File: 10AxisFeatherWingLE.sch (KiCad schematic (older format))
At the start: 19 parts, among them J1 feather long, J2 feather short, J3 grove connector, J4 feather long, J5 feather short, J6 feather breakout, U1 LSM9DS1, U2 BMP280

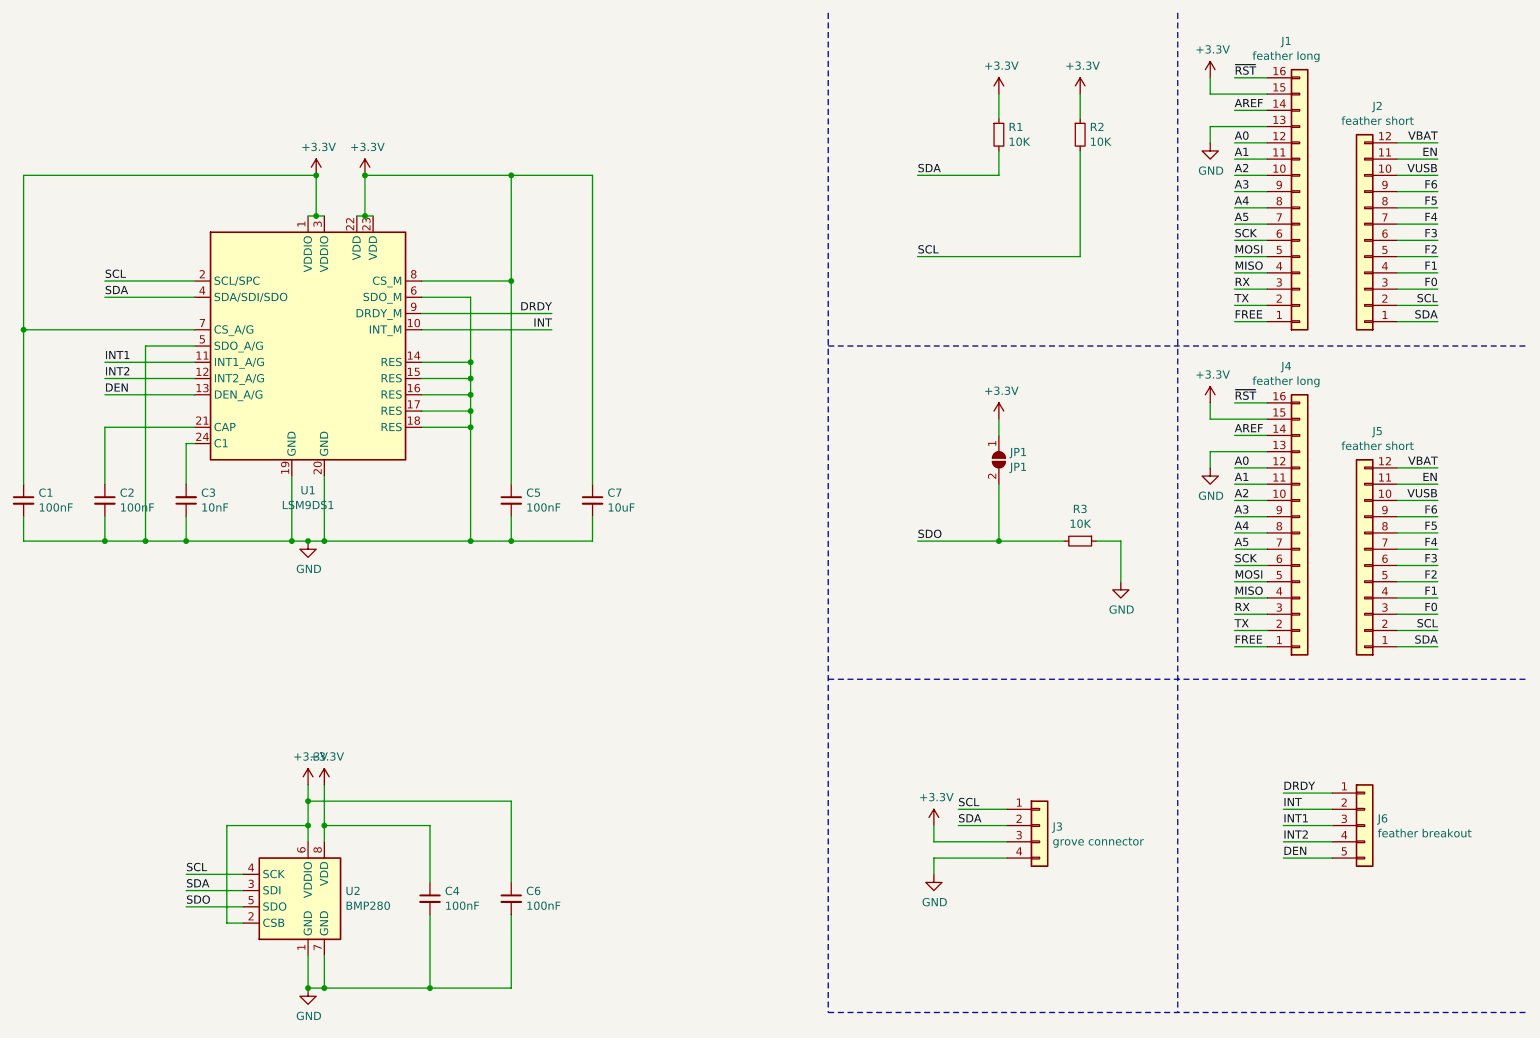
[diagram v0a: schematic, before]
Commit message: Corrected capacitor values
CAP and C1 capacitors were flipped, fixed
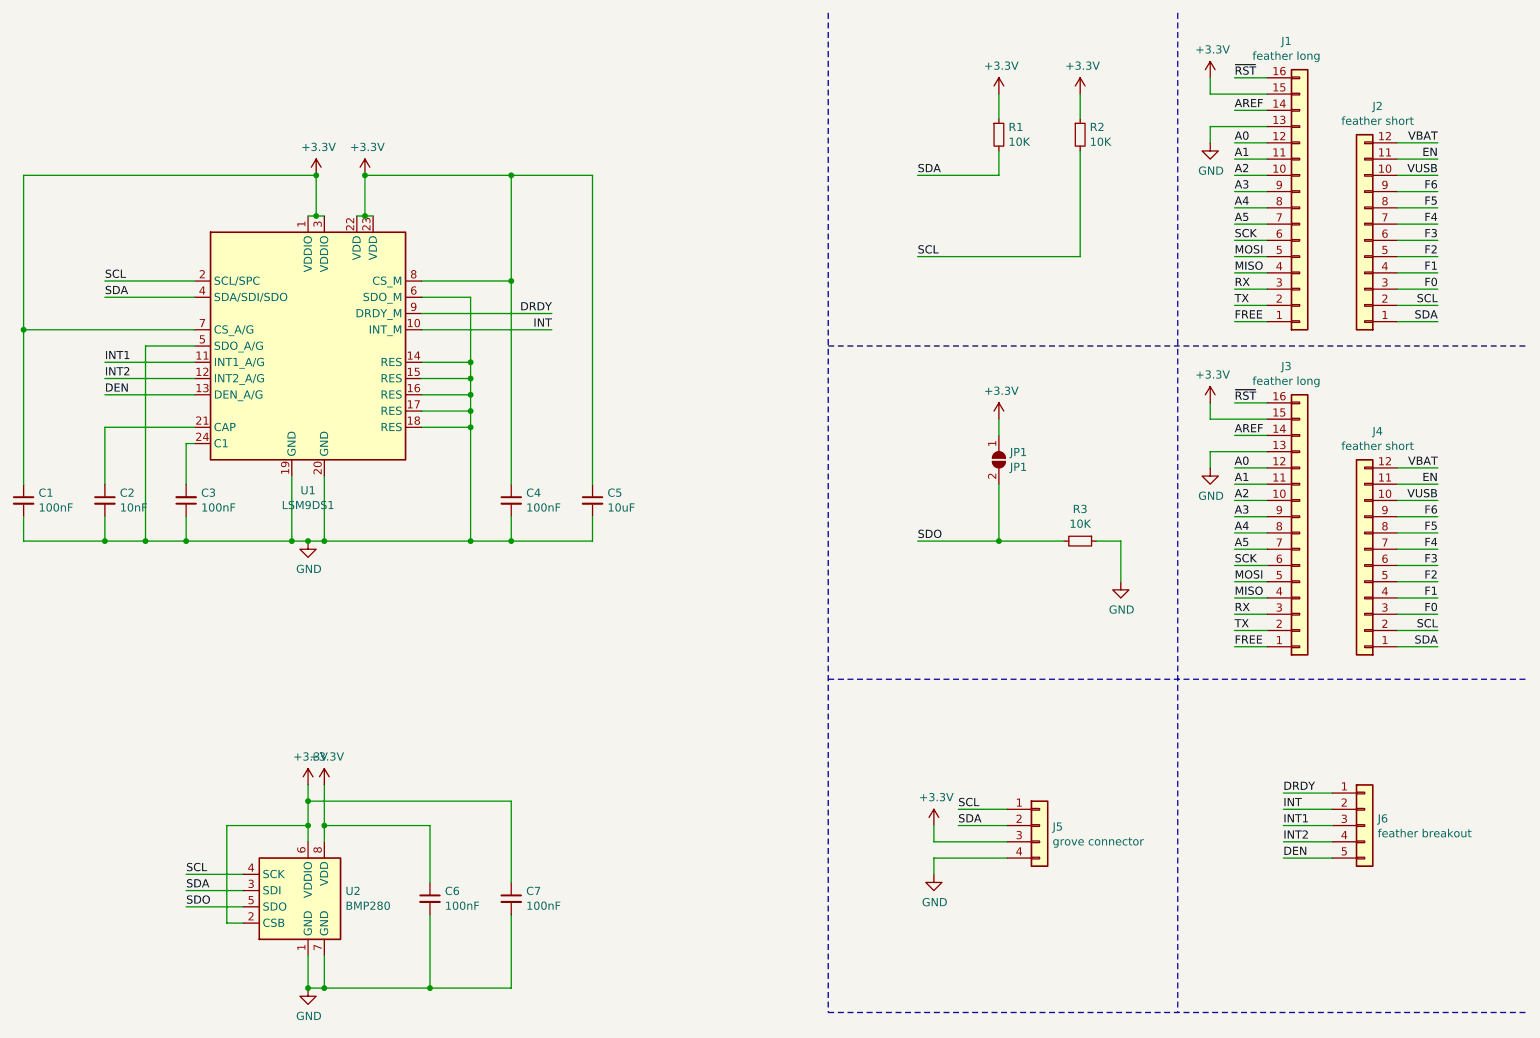
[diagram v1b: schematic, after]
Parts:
- C2: value 100nF -> 10nF
- C3: value 10nF -> 100nF
- J3: renamed from J4; footprint Connector_PinHeader_2.54mm:PinHeader_1x16_P2.54mm_Vertical -> Connector_PinSocket_2.54mm:PinSocket_1x16_P2.54mm_Vertical
- J4: renamed from J5; footprint Connector_PinHeader_2.54mm:PinHeader_1x12_P2.54mm_Vertical -> Connector_PinSocket_2.54mm:PinSocket_1x12_P2.54mm_Vertical
- renumbered C5 to C4, C7 to C5, C4 to C6, C6 to C7, J3 to J5
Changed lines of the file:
@@
 $EndComp
 $Comp
-L power:GND #PWR02
+L power:GND #PWR04
 U 1 1 5D3787E4
 P 8550 1300
-F 0 "#PWR02" H 8550 1050 50  0001 C CNN
+F 0 "#PWR04" H 8550 1050 50  0001 C CNN
 F 1 "GND" H 8555 1127 50  0000 C CNN
 F 2 "" H 8550 1300 50  0001 C CNN
@@
 	6200 500  6200 6650
 $Comp
-L Connector_Generic:Conn_01x16 J4
+L Connector_Generic:Conn_01x16 J3
 U 1 1 5E0C551A
 P 9100 3700
-F 0 "J4" H 9019 2675 50  0000 C CNN
+F 0 "J3" H 9019 2675 50  0000 C CNN
 F 1 "feather long" H 9019 2766 50  0000 C CNN
-F 2 "Connector_PinHeader_2.54mm:PinHeader_1x16_P2.54mm_Vertical" H 9100 3700 50  0001 C CNN
+F 2 "Connector_PinSocket_2.54mm:PinSocket_1x16_P2.54mm_Vertical" H 9100 3700 50  0001 C CNN
 F 3 "~" H 9100 3700 50  0001 C CNN
 	1    9100 3700
@@
 $EndComp
 $Comp
-L Connector_Generic:Conn_01x12 J5
+L Connector_Generic:Conn_01x12 J4
 U 1 1 5E0C5520
 P 9500 3900
-F 0 "J5" H 9420 3075 50  0000 C CNN
+F 0 "J4" H 9420 3075 50  0000 C CNN
 F 1 "feather short" H 9420 3166 50  0000 C CNN
-F 2 "Connector_PinHeader_2.54mm:PinHeader_1x12_P2.54mm_Vertical" H 9500 3900 50  0001 C CNN
+F 2 "Connector_PinSocket_2.54mm:PinSocket_1x12_P2.54mm_Vertical" H 9500 3900 50  0001 C CNN
 F 3 "~" H 9500 3900 50  0001 C CNN
 	1    9500 3900
@@
 	9700 4400 9950 4400
 $Comp
-L power:+3.3V #PWR015
+L power:+3.3V #PWR07
 U 1 1 5E0C555A
 P 8550 2900
-F 0 "#PWR015" H 8550 2750 50  0001 C CNN
+F 0 "#PWR07" H 8550 2750 50  0001 C CNN
 F 1 "+3.3V" H 8565 3073 50  0000 C CNN
 F 2 "" H 8550 2900 50  0001 C CNN
@@
 $EndComp
 $Comp
-L power:GND #PWR016
+L power:GND #PWR09
 U 1 1 5E0C5560
 P 8550 3300
-F 0 "#PWR016" H 8550 3050 50  0001 C CNN
+F 0 "#PWR09" H 8550 3050 50  0001 C CNN
 F 1 "GND" H 8555 3127 50  0000 C CNN
 F 2 "" H 8550 3300 50  0001 C CNN
@@
 P 2250 3500
 F 0 "C3" H 2158 3454 50  0000 R CNN
-F 1 "10nF" H 2158 3545 50  0000 R CNN
+F 1 "100nF" H 2158 3545 50  0000 R CNN
 F 2 "Capacitor_SMD:C_0603_1608Metric" H 2250 3500 50  0001 C CNN
 F 3 "~" H 2250 3500 50  0001 C CNN
@@
 P 1750 3500
 F 0 "C2" H 1842 3546 50  0000 L CNN
-F 1 "100nF" H 1842 3455 50  0000 L CNN
+F 1 "10nF" H 1842 3455 50  0000 L CNN
 F 2 "Capacitor_SMD:C_0603_1608Metric" H 1750 3500 50  0001 C CNN
 F 3 "~" H 1750 3500 50  0001 C CNN
@@
 	1750 3050 1750 3400
 $Comp
-L Device:C_Small C5
+L Device:C_Small C4
 U 1 1 5E10D342
 P 4250 3500
-F 0 "C5" H 4342 3546 50  0000 L CNN
+F 0 "C4" H 4342 3546 50  0000 L CNN
 F 1 "100nF" H 4342 3455 50  0000 L CNN
 F 2 "Capacitor_SMD:C_0603_1608Metric" H 4250 3500 50  0001 C CNN
@@
 $EndComp
 $Comp
-L Device:C_Small C7
+L Device:C_Small C5
 U 1 1 5E1105B8
 P 4750 3500
-F 0 "C7" H 4842 3546 50  0000 L CNN
+F 0 "C5" H 4842 3546 50  0000 L CNN
 F 1 "10uF" H 4842 3455 50  0000 L CNN
 F 2 "Capacitor_SMD:C_0603_1608Metric" H 4750 3500 50  0001 C CNN
@@
 	3050 1500 1250 1500
 $Comp
-L power:+3.3V #PWR08
+L power:+3.3V #PWR06
 U 1 1 5E11B1B7
 P 3350 1500
-F 0 "#PWR08" H 3350 1350 50  0001 C CNN
+F 0 "#PWR06" H 3350 1350 50  0001 C CNN
 F 1 "+3.3V" H 3365 1673 50  0000 C CNN
 F 2 "" H 3350 1500 50  0001 C CNN
@@
 $EndComp
 $Comp
-L power:+3.3V #PWR06
+L power:+3.3V #PWR05
 U 1 1 5E11AD9E
 P 3050 1500
-F 0 "#PWR06" H 3050 1350 50  0001 C CNN
+F 0 "#PWR05" H 3050 1350 50  0001 C CNN
 F 1 "+3.3V" H 3065 1673 50  0000 C CNN
 F 2 "" H 3050 1500 50  0001 C CNN
@@
 	1250 1500 1250 2450
 $Comp
-L power:GND #PWR03
+L power:GND #PWR010
 U 1 1 5E0C71B1
 P 3000 3750
-F 0 "#PWR03" H 3000 3500 50  0001 C CNN
+F 0 "#PWR010" H 3000 3500 50  0001 C CNN
 F 1 "GND" H 3005 3577 50  0000 C CNN
 F 2 "" H 3000 3750 50  0001 C CNN
@@
 	3000 3750 3100 3750
 $Comp
-L Device:C_Small C4
+L Device:C_Small C6
 U 1 1 5E1BEDBD
 P 3750 5950
-F 0 "C4" H 3842 5996 50  0000 L CNN
+F 0 "C6" H 3842 5996 50  0000 L CNN
 F 1 "100nF" H 3842 5905 50  0000 L CNN
 F 2 "Capacitor_SMD:C_0603_1608Metric" H 3750 5950 50  0001 C CNN
@@
 $EndComp
 $Comp
-L Device:C_Small C6
+L Device:C_Small C7
 U 1 1 5E1BF420
 P 4250 5950
-F 0 "C6" H 4342 5996 50  0000 L CNN
+F 0 "C7" H 4342 5996 50  0000 L CNN
 F 1 "100nF" H 4342 5905 50  0000 L CNN
 F 2 "Capacitor_SMD:C_0603_1608Metric" H 4250 5950 50  0001 C CNN
@@
 $EndComp
 $Comp
-L power:+3.3V #PWR04
+L power:+3.3V #PWR012
 U 1 1 5E1BF745
 P 3000 5250
-F 0 "#PWR04" H 3000 5100 50  0001 C CNN
+F 0 "#PWR012" H 3000 5100 50  0001 C CNN
 F 1 "+3.3V" H 3015 5423 50  0000 C CNN
 F 2 "" H 3000 5250 50  0001 C CNN
@@
 $EndComp
 $Comp
-L power:+3.3V #PWR07
+L power:+3.3V #PWR013
 U 1 1 5E1BFA3F
 P 3100 5250
-F 0 "#PWR07" H 3100 5100 50  0001 C CNN
+F 0 "#PWR013" H 3100 5100 50  0001 C CNN
 F 1 "+3.3V" H 3115 5423 50  0000 C CNN
 F 2 "" H 3100 5250 50  0001 C CNN
@@
 Connection ~ 3750 6500
 $Comp
-L power:GND #PWR05
+L power:GND #PWR016
 U 1 1 5E1E9755
 P 3000 6500
-F 0 "#PWR05" H 3000 6250 50  0001 C CNN
+F 0 "#PWR016" H 3000 6250 50  0001 C CNN
 F 1 "GND" H 3005 6327 50  0000 C CNN
 F 2 "" H 3000 6500 50  0001 C CNN
@@
 	3750 5500 3750 5850
 $Comp
-L power:+3.3V #PWR011
+L power:+3.3V #PWR02
 U 1 1 5E25A615
 P 7250 1000
-F 0 "#PWR011" H 7250 850 50  0001 C CNN
+F 0 "#PWR02" H 7250 850 50  0001 C CNN
 F 1 "+3.3V" H 7265 1173 50  0000 C CNN
 F 2 "" H 7250 1000 50  0001 C CNN
@@
 $EndComp
 $Comp
-L power:+3.3V #PWR013
+L power:+3.3V #PWR03
 U 1 1 5E25A95F
 P 7750 1000
-F 0 "#PWR013" H 7750 850 50  0001 C CNN
+F 0 "#PWR03" H 7750 850 50  0001 C CNN
 F 1 "+3.3V" H 7765 1173 50  0000 C CNN
 F 2 "" H 7750 1000 50  0001 C CNN
@@
 	7250 3750 7650 3750
 $Comp
-L power:+3.3V #PWR012
+L power:+3.3V #PWR08
 U 1 1 5E2A6AB5
 P 7250 3000
-F 0 "#PWR012" H 7250 2850 50  0001 C CNN
+F 0 "#PWR08" H 7250 2850 50  0001 C CNN
 F 1 "+3.3V" H 7265 3173 50  0000 C CNN
 F 2 "" H 7250 3000 50  0001 C CNN
@@
 $EndComp
 $Comp
-L power:GND #PWR014
+L power:GND #PWR011
 U 1 1 5E2A6E98
 P 8000 4000
-F 0 "#PWR014" H 8000 3750 50  0001 C CNN
+F 0 "#PWR011" H 8000 3750 50  0001 C CNN
 F 1 "GND" H 8005 3827 50  0000 C CNN
 F 2 "" H 8000 4000 50  0001 C CNN
@@
 SDO
 $Comp
-L Connector_Generic:Conn_01x04 J3
+L Connector_Generic:Conn_01x04 J5
 U 1 1 5E2B8C1A
 P 7500 5500
-F 0 "J3" H 7580 5492 50  0000 L CNN
+F 0 "J5" H 7580 5492 50  0000 L CNN
 F 1 "grove connector" H 7580 5401 50  0000 L CNN
 F 2 "Connector:NS-Tech_Grove_1x04_P2mm_Vertical" H 7500 5500 50  0001 C CNN
@@
 	6850 5700 7300 5700
 $Comp
-L power:+3.3V #PWR09
+L power:+3.3V #PWR014
 U 1 1 5E330536
 P 6850 5500
-F 0 "#PWR09" H 6850 5350 50  0001 C CNN
+F 0 "#PWR014" H 6850 5350 50  0001 C CNN
 F 1 "+3.3V" H 6865 5673 50  0000 C CNN
 F 2 "" H 6850 5500 50  0001 C CNN
@@
 $EndComp
 $Comp
-L power:GND #PWR010
+L power:GND #PWR015
 U 1 1 5E330953
 P 6850 5800
-F 0 "#PWR010" H 6850 5550 50  0001 C CNN
+F 0 "#PWR015" H 6850 5550 50  0001 C CNN
 F 1 "GND" H 6855 5627 50  0000 C CNN
 F 2 "" H 6850 5800 50  0001 C CNN

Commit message: Minor format fix
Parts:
- added H1, H2, H3, H4: MountingHole, MountingHole:MountingHole_2.7mm_M2.5, symbol Mechanical:MountingHole
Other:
- moved on the sheet: J6
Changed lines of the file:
@@
 L Connector_Generic:Conn_01x05 J6
 U 1 1 5E2059E9
-P 9500 5500
-F 0 "J6" H 9580 5542 50  0000 L CNN
-F 1 "feather breakout" H 9580 5451 50  0000 L CNN
-F 2 "Connector_PinHeader_2.54mm:PinHeader_1x05_P2.54mm_Vertical" H 9500 5500 50  0001 C CNN
-F 3 "~" H 9500 5500 50  0001 C CNN
-	1    9500 5500
-	1    0    0    -1
-$EndComp
-Text Label 9000 5300 0    50   ~ 0
+P 9550 5000
+F 0 "J6" H 9630 5042 50  0000 L CNN
+F 1 "feather breakout" H 9630 4951 50  0000 L CNN
+F 2 "Connector_PinHeader_2.54mm:PinHeader_1x05_P2.54mm_Vertical" H 9550 5000 50  0001 C CNN
+F 3 "~" H 9550 5000 50  0001 C CNN
+	1    9550 5000
+	1    0    0    -1
+$EndComp
+Text Label 9050 4800 0    50   ~ 0
 DRDY
-Text Label 9000 5400 0    50   ~ 0
+Text Label 9050 4900 0    50   ~ 0
 INT
-Text Label 9000 5500 0    50   ~ 0
+Text Label 9050 5000 0    50   ~ 0
 INT1
-Text Label 9000 5600 0    50   ~ 0
+Text Label 9050 5100 0    50   ~ 0
 INT2
-Text Label 9000 5700 0    50   ~ 0
+Text Label 9050 5200 0    50   ~ 0
 DEN
 Wire Wire Line
@@
 $EndComp
 Wire Wire Line
-	9000 5300 9300 5300
-Wire Wire Line
-	9000 5400 9300 5400
-Wire Wire Line
-	9000 5500 9300 5500
-Wire Wire Line
-	9000 5600 9300 5600
-Wire Wire Line
-	9000 5700 9300 5700
+	9050 4800 9350 4800
+Wire Wire Line
+	9050 4900 9350 4900
+Wire Wire Line
+	9050 5000 9350 5000
+Wire Wire Line
+	9050 5100 9350 5100
+Wire Wire Line
+	9050 5200 9350 5200
 Wire Wire Line
 	7000 5400 7300 5400
@@
 	1    0    0    -1
 $EndComp
+$Comp
+L Mechanical:MountingHole H1
+U 1 1 5E162FA6
+P 9250 5750
+F 0 "H1" H 9350 5796 50  0000 L CNN
+F 1 "MountingHole" H 9350 5705 50  0000 L CNN
+F 2 "MountingHole:MountingHole_2.7mm_M2.5" H 9250 5750 50  0001 C CNN
+F 3 "~" H 9250 5750 50  0001 C CNN
+	1    9250 5750
+	1    0    0    -1
+$EndComp
+$Comp
+L Mechanical:MountingHole H2
+U 1 1 5E163654
+P 9250 6000
+F 0 "H2" H 9350 6046 50  0000 L CNN
+F 1 "MountingHole" H 9350 5955 50  0000 L CNN
+F 2 "MountingHole:MountingHole_2.7mm_M2.5" H 9250 6000 50  0001 C CNN
+F 3 "~" H 9250 6000 50  0001 C CNN
+	1    9250 6000
+	1    0    0    -1
+$EndComp
+$Comp
+L Mechanical:MountingHole H3
+U 1 1 5E163A5D
+P 9250 6250
+F 0 "H3" H 9350 6296 50  0000 L CNN
+F 1 "MountingHole" H 9350 6205 50  0000 L CNN
+F 2 "MountingHole:MountingHole_2.7mm_M2.5" H 9250 6250 50  0001 C CNN
+F 3 "~" H 9250 6250 50  0001 C CNN
+	1    9250 6250
+	1    0    0    -1
+$EndComp
+$Comp
+L Mechanical:MountingHole H4
+U 1 1 5E163E72
+P 9250 6500
+F 0 "H4" H 9350 6546 50  0000 L CNN
+F 1 "MountingHole" H 9350 6455 50  0000 L CNN
+F 2 "MountingHole:MountingHole_2.7mm_M2.5" H 9250 6500 50  0001 C CNN
+F 3 "~" H 9250 6500 50  0001 C CNN
+	1    9250 6500
+	1    0    0    -1
+$EndComp
+Wire Notes Line
+	8350 5500 10500 5500
 $EndSCHEMATC

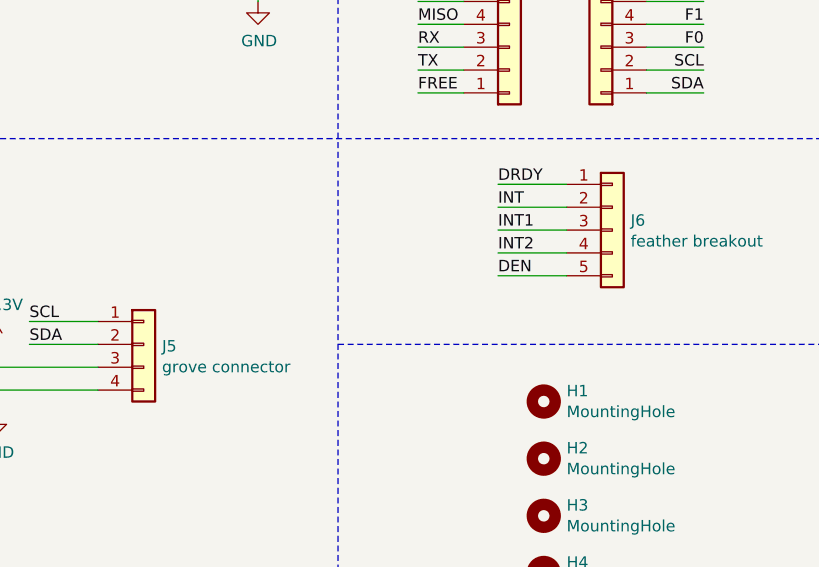
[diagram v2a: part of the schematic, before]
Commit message: Increased trace width
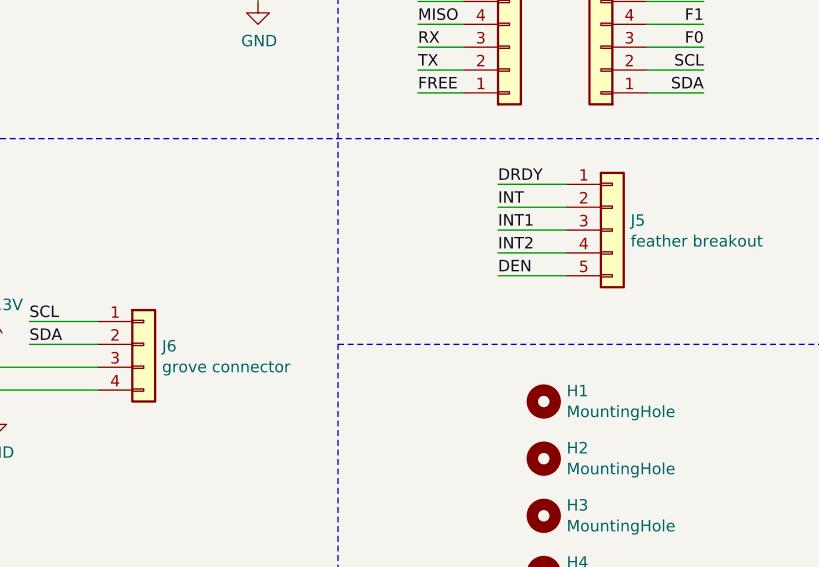
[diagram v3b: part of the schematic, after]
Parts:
- renumbered J6 to J5, J5 to J6
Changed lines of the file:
@@
 SDO
 $Comp
-L Connector_Generic:Conn_01x05 J6
+L Connector_Generic:Conn_01x05 J5
 U 1 1 5E2059E9
 P 9550 5000
-F 0 "J6" H 9630 5042 50  0000 L CNN
+F 0 "J5" H 9630 5042 50  0000 L CNN
 F 1 "feather breakout" H 9630 4951 50  0000 L CNN
 F 2 "Connector_PinHeader_2.54mm:PinHeader_1x05_P2.54mm_Vertical" H 9550 5000 50  0001 C CNN
@@
 SDO
 $Comp
-L Connector_Generic:Conn_01x04 J5
+L Connector_Generic:Conn_01x04 J6
 U 1 1 5E2B8C1A
 P 7500 5500
-F 0 "J5" H 7580 5492 50  0000 L CNN
+F 0 "J6" H 7580 5492 50  0000 L CNN
 F 1 "grove connector" H 7580 5401 50  0000 L CNN
 F 2 "Connector:NS-Tech_Grove_1x04_P2mm_Vertical" H 7500 5500 50  0001 C CNN

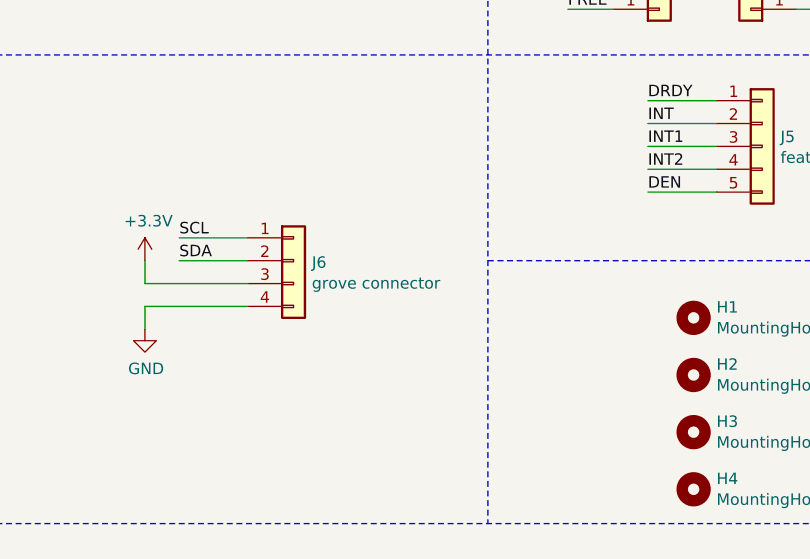
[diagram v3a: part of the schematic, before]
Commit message: Changed grove connector to STEMMA
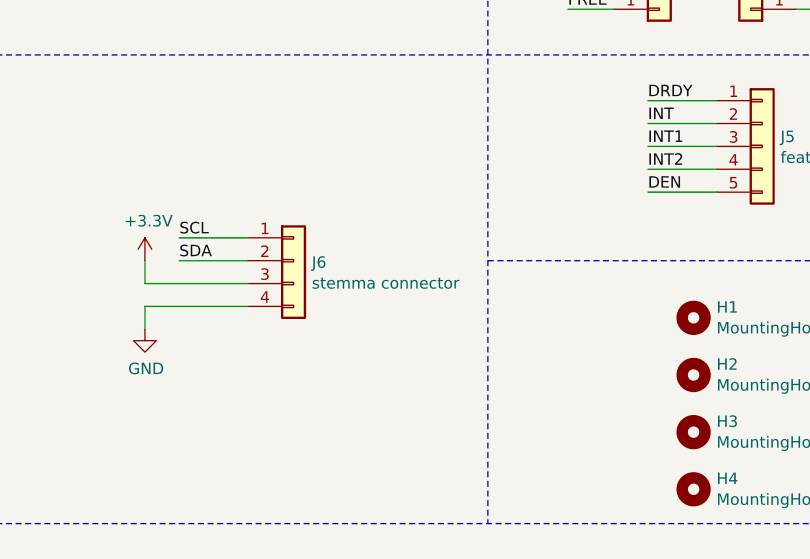
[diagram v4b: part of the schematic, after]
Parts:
- J6: value grove connector -> stemma connector; footprint Connector:NS-Tech_Grove_1x04_P2mm_Vertical -> Connector_JST:JST_PH_B4B-PH-K_1x04_P2.00mm_Vertical
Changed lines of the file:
@@
 P 7500 5500
 F 0 "J6" H 7580 5492 50  0000 L CNN
-F 1 "grove connector" H 7580 5401 50  0000 L CNN
-F 2 "Connector:NS-Tech_Grove_1x04_P2mm_Vertical" H 7500 5500 50  0001 C CNN
+F 1 "stemma connector" H 7580 5401 50  0000 L CNN
+F 2 "Connector_JST:JST_PH_B4B-PH-K_1x04_P2.00mm_Vertical" H 7500 5500 50  0001 C CNN
 F 3 "~" H 7500 5500 50  0001 C CNN
 	1    7500 5500
